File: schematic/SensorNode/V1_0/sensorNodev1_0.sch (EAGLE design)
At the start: 32 parts, among them IC1 V_REG_MIC2920, IC2 SI7021-A10-GM, J1 AVR_SPI_PRG_62X3_LOCK, U1 ATMEGA328P_TQFP, U2 ADA4077-1ARZ

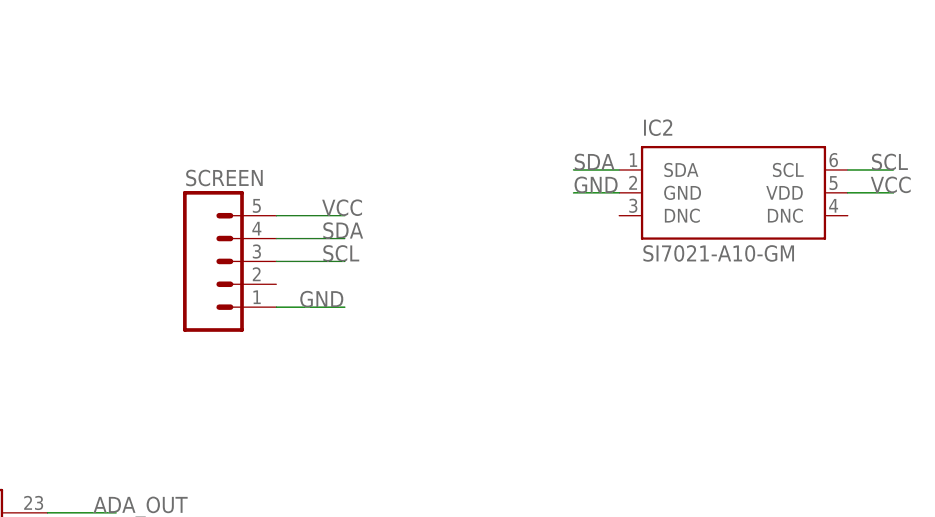
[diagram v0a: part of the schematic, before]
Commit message: Replacing Screen connector with low profile Jst-EH connector
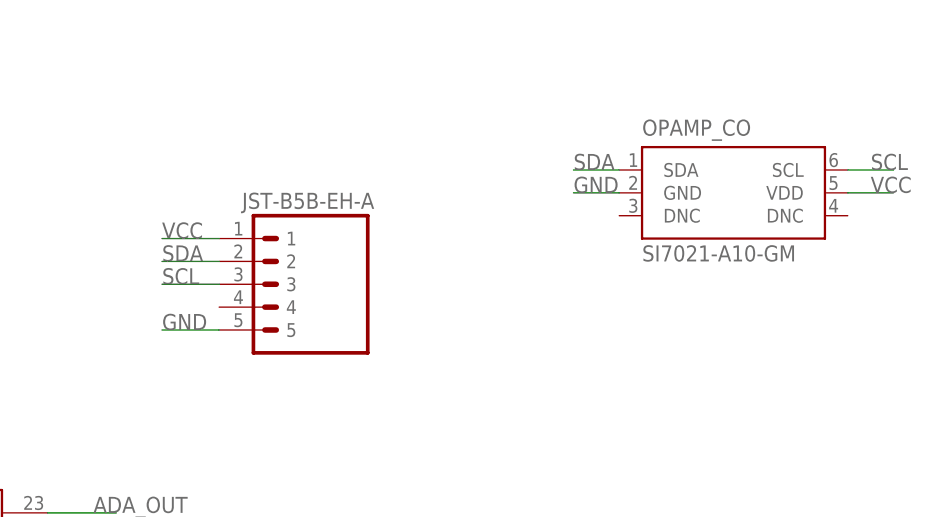
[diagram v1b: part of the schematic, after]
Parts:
- SCREEN: value (none) -> JST-B5B-EH-A; device SparkFun-Connectors:M05PTH -> bespin:JST-B5B-EH-A
- renumbered IC2 to OPAMP_CO, JP3 to CO2
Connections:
- net GND: now also SCREEN.5; no longer SCREEN.1
- net SDA: now also SCREEN.2; no longer SCREEN.4
- net VCC: now also SCREEN.1; no longer SCREEN.5
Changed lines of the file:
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@@
 <part name="GND11" library="SparkFun-Aesthetics" deviceset="GND" device=""/>
 <part name="PWR" library="SparkFun-LED" deviceset="LED" device="0603"/>
-<part name="JP3" library="bespin" deviceset="K-30" device="K-30"/>
-<part name="SCREEN" library="SparkFun-Connectors" deviceset="M05" device="PTH"/>
+<part name="CO2" library="bespin" deviceset="K-30" device="K-30"/>
 <part name="ENTER" library="SparkFun-Electromechanical" deviceset="SWITCH-MOMENTARY-2" device="PTH"/>
 <part name="BACK" library="SparkFun-Electromechanical" deviceset="SWITCH-MOMENTARY-2" device="PTH"/>
@@
 <part name="C6" library="SparkFun-Capacitors" deviceset="22PF-50V-5%(0603)" device="" value="22pF"/>
 <part name="U$2" library="bespin" deviceset="NRF24L01" device=""/>
-<part name="IC2" library="bespin" deviceset="SI7021-*" device="" technology="A10-GM"/>
+<part name="OPAMP_CO" library="bespin" deviceset="SI7021-*" device="" technology="A10-GM"/>
+<part name="SCREEN" library="bespin" deviceset="JST-B5B-EH-A" device=""/>
 </parts>
 <sheets>
@@
 <instance part="GND11" gate="1" x="154.94" y="45.72"/>
 <instance part="PWR" gate="G$1" x="154.94" y="58.42"/>
-<instance part="JP3" gate="G$1" x="218.44" y="104.14"/>
-<instance part="SCREEN" gate="G$1" x="154.94" y="157.48"/>
+<instance part="CO2" gate="G$1" x="218.44" y="104.14"/>
 <instance part="ENTER" gate="G$1" x="116.84" y="180.34" smashed="yes"/>
 <instance part="BACK" gate="G$1" x="116.84" y="172.72" smashed="yes"/>
@@
 <instance part="C6" gate="G$1" x="83.82" y="12.7"/>
 <instance part="U$2" gate="A" x="213.36" y="50.8"/>
-<instance part="IC2" gate="G$1" x="213.36" y="165.1"/>
+<instance part="OPAMP_CO" gate="G$1" x="213.36" y="165.1"/>
+<instance part="SCREEN" gate="JST-5" x="160.02" y="147.32"/>
 </instances>
 <busses>
@@
 </segment>
 <segment>
-<pinref part="SCREEN" gate="G$1" pin="5"/>
-<wire x1="162.56" y1="162.56" x2="170.18" y2="162.56" width="0.1524" layer="91"/>
-<label x="167.64" y="162.56" size="1.778" layer="95"/>
-</segment>
-<segment>
 <pinref part="SUPPLY5" gate="G$1" pin="VCC"/>
 <wire x1="96.52" y1="154.94" x2="96.52" y2="157.48" width="0.1524" layer="91"/>
@@
 </segment>
 <segment>
-<pinref part="IC2" gate="G$1" pin="VDD"/>
+<pinref part="OPAMP_CO" gate="G$1" pin="VDD"/>
 <wire x1="226.06" y1="165.1" x2="231.14" y2="165.1" width="0.1524" layer="91"/>
 <label x="228.6" y="165.1" size="1.778" layer="95"/>
+</segment>
+<segment>
+<pinref part="SCREEN" gate="JST-5" pin="1"/>
+<wire x1="156.21" y1="160.02" x2="149.86" y2="160.02" width="0.1524" layer="91"/>
+<label x="149.86" y="160.02" size="1.778" layer="95"/>
 </segment>
 </net>
@@
 </segment>
 <segment>
-<pinref part="JP3" gate="G$1" pin="GND@2"/>
+<pinref part="CO2" gate="G$1" pin="GND@2"/>
 <wire x1="226.06" y1="104.14" x2="231.14" y2="104.14" width="0.1524" layer="91"/>
 <label x="228.6" y="104.14" size="1.778" layer="95"/>
-</segment>
-<segment>
-<pinref part="SCREEN" gate="G$1" pin="1"/>
-<wire x1="162.56" y1="152.4" x2="170.18" y2="152.4" width="0.1524" layer="91"/>
-<label x="165.1" y="152.4" size="1.778" layer="95"/>
 </segment>
 <segment>
@@
 </segment>
 <segment>
-<pinref part="IC2" gate="G$1" pin="GND"/>
+<pinref part="OPAMP_CO" gate="G$1" pin="GND"/>
 <wire x1="200.66" y1="165.1" x2="195.58" y2="165.1" width="0.1524" layer="91"/>
 <label x="195.58" y="165.1" size="1.778" layer="95"/>
+</segment>
+<segment>
+<pinref part="SCREEN" gate="JST-5" pin="5"/>
+<wire x1="156.21" y1="149.86" x2="149.86" y2="149.86" width="0.1524" layer="91"/>
+<label x="149.86" y="149.86" size="1.778" layer="95"/>
 </segment>
 </net>
@@
 </segment>
 <segment>
-<pinref part="SCREEN" gate="G$1" pin="4"/>
-<wire x1="162.56" y1="160.02" x2="170.18" y2="160.02" width="0.1524" layer="91"/>
-<label x="167.64" y="160.02" size="1.778" layer="95"/>
-</segment>
-<segment>
-<pinref part="IC2" gate="G$1" pin="SDA"/>
+<pinref part="OPAMP_CO" gate="G$1" pin="SDA"/>
 <wire x1="200.66" y1="167.64" x2="195.58" y2="167.64" width="0.1524" layer="91"/>
 <label x="195.58" y="167.64" size="1.778" layer="95"/>
+</segment>
+<segment>
+<pinref part="SCREEN" gate="JST-5" pin="2"/>
+<wire x1="156.21" y1="157.48" x2="149.86" y2="157.48" width="0.1524" layer="91"/>
+<label x="149.86" y="157.48" size="1.778" layer="95"/>
 </segment>
 </net>
@@
 </segment>
 <segment>
-<pinref part="SCREEN" gate="G$1" pin="3"/>
-<wire x1="162.56" y1="157.48" x2="170.18" y2="157.48" width="0.1524" layer="91"/>
-<label x="167.64" y="157.48" size="1.778" layer="95"/>
-</segment>
-<segment>
-<pinref part="IC2" gate="G$1" pin="SCL"/>
+<pinref part="OPAMP_CO" gate="G$1" pin="SCL"/>
 <wire x1="226.06" y1="167.64" x2="231.14" y2="167.64" width="0.1524" layer="91"/>
 <label x="228.6" y="167.64" size="1.778" layer="95"/>
+</segment>
+<segment>
+<pinref part="SCREEN" gate="JST-5" pin="3"/>
+<wire x1="156.21" y1="154.94" x2="149.86" y2="154.94" width="0.1524" layer="91"/>
+<label x="149.86" y="154.94" size="1.778" layer="95"/>
 </segment>
 </net>
@@
 </segment>
 <segment>
-<pinref part="JP3" gate="G$1" pin="VCC"/>
+<pinref part="CO2" gate="G$1" pin="VCC"/>
 <wire x1="187.96" y1="99.06" x2="182.88" y2="99.06" width="0.1524" layer="91"/>
 <label x="182.88" y="99.06" size="1.778" layer="95"/>
@@
 <net name="TX_K30" class="0">
 <segment>
-<pinref part="JP3" gate="G$1" pin="RXD_U"/>
+<pinref part="CO2" gate="G$1" pin="RXD_U"/>
 <wire x1="187.96" y1="86.36" x2="180.34" y2="86.36" width="0.1524" layer="91"/>
 <label x="177.8" y="86.36" size="1.778" layer="95"/>
@@
 <net name="RX_K30" class="0">
 <segment>
-<pinref part="JP3" gate="G$1" pin="TXD_U"/>
+<pinref part="CO2" gate="G$1" pin="TXD_U"/>
 <wire x1="226.06" y1="88.9" x2="233.68" y2="88.9" width="0.1524" layer="91"/>
 <label x="228.6" y="88.9" size="1.778" layer="95"/>

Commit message: Update to Schematics o Adding light sensor schematic o Added light sensor connector for sensor node o Split part libraries to common and schematic specific
 and surface mount Tmp/Hum module
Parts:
- removed OPAMP_CO: SI7021-A10-GM, bespin:SI7021-A10-GM
- added C7: 0.1uF, SparkFun-Capacitors:0.1UF-25V(+80/-20%)(0603)
- added IC2: SI7021-A10-IM, si70xx-10:SI7021-A10-IM
- added LIGHT: JST-B4B-EH-A, duppy_common:JST-B4B-EH-A
- BACK, DOWN, ENTER, UP: value SWITCH-MOMENTARY-2PTH -> SWITCH-MOMENTARY-2SIDE_EZ; device SparkFun-Electromechanical:SWITCH-MOMENTARY-2PTH -> SparkFun-Electromechanical:SWITCH-MOMENTARY-2SIDE_EZ
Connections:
- removed net DTHP: U1.PC3(ADC3)
- net GND: now also C7.1, IC2.GND, LIGHT.4; no longer OPAMP_CO.GND
- net SCL: now also IC2.SCL, LIGHT.3; no longer OPAMP_CO.SCL
- net SDA: now also IC2.SDA, LIGHT.2; no longer OPAMP_CO.SDA
- net VCC: now also C7.2, IC2.VDD, LIGHT.1; no longer OPAMP_CO.VDD
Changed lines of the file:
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@@
 <part name="PWR" library="SparkFun-LED" deviceset="LED" device="0603"/>
 <part name="CO2" library="bespin" deviceset="K-30" device="K-30"/>
-<part name="ENTER" library="SparkFun-Electromechanical" deviceset="SWITCH-MOMENTARY-2" device="PTH"/>
-<part name="BACK" library="SparkFun-Electromechanical" deviceset="SWITCH-MOMENTARY-2" device="PTH"/>
-<part name="UP" library="SparkFun-Electromechanical" deviceset="SWITCH-MOMENTARY-2" device="PTH"/>
-<part name="DOWN" library="SparkFun-Electromechanical" deviceset="SWITCH-MOMENTARY-2" device="PTH"/>
+<part name="ENTER" library="SparkFun-Electromechanical" deviceset="SWITCH-MOMENTARY-2" device="SIDE_EZ" value="SWITCH-MOMENTARY-2SIDE_EZ"/>
+<part name="BACK" library="SparkFun-Electromechanical" deviceset="SWITCH-MOMENTARY-2" device="SIDE_EZ" value="SWITCH-MOMENTARY-2SIDE_EZ"/>
+<part name="UP" library="SparkFun-Electromechanical" deviceset="SWITCH-MOMENTARY-2" device="SIDE_EZ" value="SWITCH-MOMENTARY-2SIDE_EZ"/>
+<part name="DOWN" library="SparkFun-Electromechanical" deviceset="SWITCH-MOMENTARY-2" device="SIDE_EZ" value="SWITCH-MOMENTARY-2SIDE_EZ"/>
 <part name="R2" library="SparkFun-Resistors" deviceset="1KOHM-1/10W-1%(0603)" device="" value="1K"/>
 <part name="R6" library="SparkFun-Resistors" deviceset="1KOHM-1/10W-1%(0603)" device="" value="1K"/>
@@
 <part name="C6" library="SparkFun-Capacitors" deviceset="22PF-50V-5%(0603)" device="" value="22pF"/>
 <part name="U$2" library="bespin" deviceset="NRF24L01" device=""/>
-<part name="OPAMP_CO" library="bespin" deviceset="SI7021-*" device="" technology="A10-GM"/>
 <part name="SCREEN" library="bespin" deviceset="JST-B5B-EH-A" device=""/>
+<part name="LIGHT" library="duppy_common" deviceset="JST-B4B-EH-A" device=""/>
+<part name="IC2" library="si70xx-10" deviceset="SI7021-*" device="" technology="A10-IM" value="SI7021-A10-IM"/>
+<part name="C7" library="SparkFun-Capacitors" deviceset="0.1UF-25V(+80/-20%)(0603)" device="" value="0.1uF"/>
+<part name="GND4" library="SparkFun-Aesthetics" deviceset="GND" device=""/>
 </parts>
 <sheets>
@@
 <instance part="C6" gate="G$1" x="83.82" y="12.7"/>
 <instance part="U$2" gate="A" x="213.36" y="50.8"/>
-<instance part="OPAMP_CO" gate="G$1" x="213.36" y="165.1"/>
 <instance part="SCREEN" gate="JST-5" x="160.02" y="147.32"/>
+<instance part="LIGHT" gate="G$1" x="198.12" y="134.62"/>
+<instance part="IC2" gate="G$1" x="205.74" y="170.18"/>
+<instance part="C7" gate="G$1" x="226.06" y="162.56" rot="R180"/>
+<instance part="GND4" gate="1" x="226.06" y="152.4"/>
 </instances>
 <busses>
@@
 </segment>
 <segment>
-<pinref part="OPAMP_CO" gate="G$1" pin="VDD"/>
-<wire x1="226.06" y1="165.1" x2="231.14" y2="165.1" width="0.1524" layer="91"/>
-<label x="228.6" y="165.1" size="1.778" layer="95"/>
-</segment>
-<segment>
 <pinref part="SCREEN" gate="JST-5" pin="1"/>
 <wire x1="156.21" y1="160.02" x2="149.86" y2="160.02" width="0.1524" layer="91"/>
 <label x="149.86" y="160.02" size="1.778" layer="95"/>
+</segment>
+<segment>
+<pinref part="LIGHT" gate="G$1" pin="1"/>
+<wire x1="194.31" y1="144.78" x2="185.42" y2="144.78" width="0.1524" layer="91"/>
+<label x="185.42" y="144.78" size="1.778" layer="95"/>
+</segment>
+<segment>
+<pinref part="IC2" gate="G$1" pin="VDD"/>
+<wire x1="218.44" y1="170.18" x2="226.06" y2="170.18" width="0.1524" layer="91"/>
+<wire x1="226.06" y1="170.18" x2="226.06" y2="165.1" width="0.1524" layer="91"/>
+<pinref part="C7" gate="G$1" pin="2"/>
+<wire x1="226.06" y1="170.18" x2="233.68" y2="170.18" width="0.1524" layer="91"/>
+<junction x="226.06" y="170.18"/>
+<label x="228.6" y="170.18" size="1.778" layer="95"/>
 </segment>
 </net>
@@
 </segment>
 <segment>
-<pinref part="OPAMP_CO" gate="G$1" pin="GND"/>
-<wire x1="200.66" y1="165.1" x2="195.58" y2="165.1" width="0.1524" layer="91"/>
-<label x="195.58" y="165.1" size="1.778" layer="95"/>
-</segment>
-<segment>
 <pinref part="SCREEN" gate="JST-5" pin="5"/>
 <wire x1="156.21" y1="149.86" x2="149.86" y2="149.86" width="0.1524" layer="91"/>
 <label x="149.86" y="149.86" size="1.778" layer="95"/>
+</segment>
+<segment>
+<pinref part="IC2" gate="G$1" pin="GND"/>
+<wire x1="193.04" y1="170.18" x2="185.42" y2="170.18" width="0.1524" layer="91"/>
+<label x="185.42" y="170.18" size="1.778" layer="95"/>
+</segment>
+<segment>
+<pinref part="LIGHT" gate="G$1" pin="4"/>
+<wire x1="194.31" y1="137.16" x2="185.42" y2="137.16" width="0.1524" layer="91"/>
+<label x="185.42" y="137.16" size="1.778" layer="95"/>
+</segment>
+<segment>
+<pinref part="C7" gate="G$1" pin="1"/>
+<wire x1="226.06" y1="157.48" x2="226.06" y2="154.94" width="0.1524" layer="91"/>
+<pinref part="GND4" gate="1" pin="GND"/>
 </segment>
 </net>
@@
 </segment>
 </net>
-<net name="DTHP" class="0">
-<segment>
-<wire x1="137.16" y1="121.92" x2="144.78" y2="121.92" width="0.1524" layer="91"/>
-<label x="142.24" y="121.92" size="1.778" layer="95"/>
-<pinref part="U1" gate="U$1" pin="PC3(ADC3)"/>
-</segment>
-</net>
 <net name="N$1" class="0">
 <segment>
@@
 </segment>
 <segment>
-<pinref part="OPAMP_CO" gate="G$1" pin="SDA"/>
-<wire x1="200.66" y1="167.64" x2="195.58" y2="167.64" width="0.1524" layer="91"/>
-<label x="195.58" y="167.64" size="1.778" layer="95"/>
-</segment>
-<segment>
 <pinref part="SCREEN" gate="JST-5" pin="2"/>
 <wire x1="156.21" y1="157.48" x2="149.86" y2="157.48" width="0.1524" layer="91"/>
 <label x="149.86" y="157.48" size="1.778" layer="95"/>
 </segment>
+<segment>
+<pinref part="IC2" gate="G$1" pin="SDA"/>
+<wire x1="193.04" y1="172.72" x2="185.42" y2="172.72" width="0.1524" layer="91"/>
+<label x="185.42" y="172.72" size="1.778" layer="95"/>
+</segment>
+<segment>
+<pinref part="LIGHT" gate="G$1" pin="2"/>
+<wire x1="194.31" y1="142.24" x2="185.42" y2="142.24" width="0.1524" layer="91"/>
+<label x="185.42" y="142.24" size="1.778" layer="95"/>
+</segment>
 </net>
 <net name="SCL" class="0">
@@
 </segment>
 <segment>
-<pinref part="OPAMP_CO" gate="G$1" pin="SCL"/>
-<wire x1="226.06" y1="167.64" x2="231.14" y2="167.64" width="0.1524" layer="91"/>
-<label x="228.6" y="167.64" size="1.778" layer="95"/>
-</segment>
-<segment>
 <pinref part="SCREEN" gate="JST-5" pin="3"/>
 <wire x1="156.21" y1="154.94" x2="149.86" y2="154.94" width="0.1524" layer="91"/>
 <label x="149.86" y="154.94" size="1.778" layer="95"/>
 </segment>
-</net>
+<segment>
+<pinref part="IC2" gate="G$1" pin="SCL"/>
+<wire x1="218.44" y1="172.72" x2="226.06" y2="172.72" width="0.1524" layer="91"/>
+<label x="223.52" y="172.72" size="1.778" layer="95"/>
+</segment>
+<segment>
+<pinref part="LIGHT" gate="G$1" pin="3"/>
+<wire x1="194.31" y1="139.7" x2="185.42" y2="139.7" width="0.1524" layer="91"/>
+<label x="185.42" y="139.7" size="1.778" layer="95"/>
+</segment>
+</net>
